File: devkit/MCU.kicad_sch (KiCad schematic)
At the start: 41 parts, among them IC601 FAN5622SX, IC602 USBLC6-2P6, IC603 MX25U51245GZ4I00, IC604 NTS0104GU12, J601 Jumper, J602 Jumper, J603 Jumper, J604 Jumper, M601 NORA-B106, X601 DEBUG, X602 Current, X603 Device, X604 UART, X605 GPIO, X606 Current, X607 IO Current, X608 Display, X609 Current, X610 LED Current

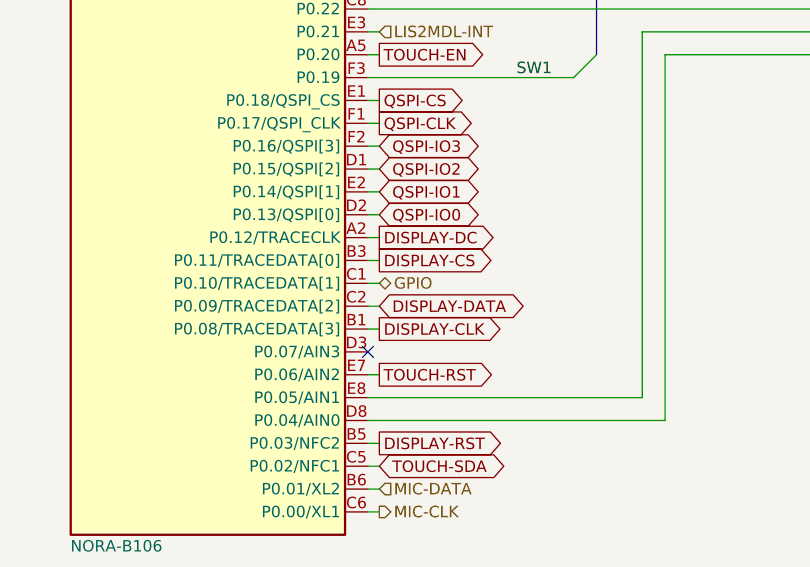
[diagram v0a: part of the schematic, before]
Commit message: Revert "Feature: Issue #180"
This reverts commit 364f4bbc8b17cbfb7f0155205af3315526997ba0.
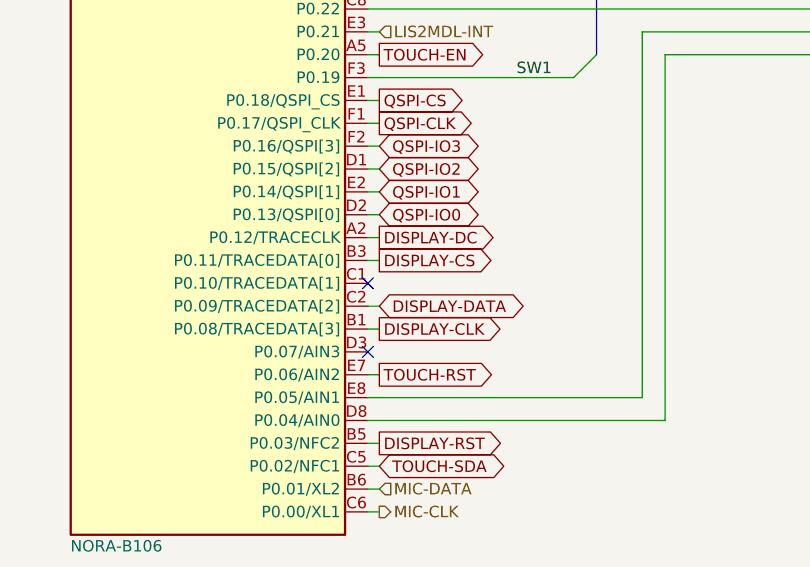
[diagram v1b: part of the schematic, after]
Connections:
- net GPIO: no longer names the net of M601.C1 (P0.10/TRACEDATA[1])
- no-connect marks 12 -> 13
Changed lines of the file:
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@@
 	)
 	(no_connect
+		(at 153.67 115.57)
+	)
+	(no_connect
 		(at 153.67 67.31)
 	)
@@
 	(wire
 		(pts
-			(xy 153.67 115.57) (xy 154.94 115.57)
-		)
-		(stroke
-			(width 0)
-			(type default)
-		)
-	)
-	(wire
-		(pts
 			(xy 124.46 181.61) (xy 124.46 210.82)
 		)
@@
 		(effects
 			(font
-				(size 1.27 1.27)
-			)
-			(justify left)
-		)
-	)
-	(hierarchical_label "GPIO"
-		(shape bidirectional)
-		(at 154.94 115.57 0)
-		(effects
-			(font

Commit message: Feature: Issue #180
- Add additional pin to I2S header

Closes #180

Signed-off-by: Daniel Kampert <DanielKampert@kampis-elektroecke.de>
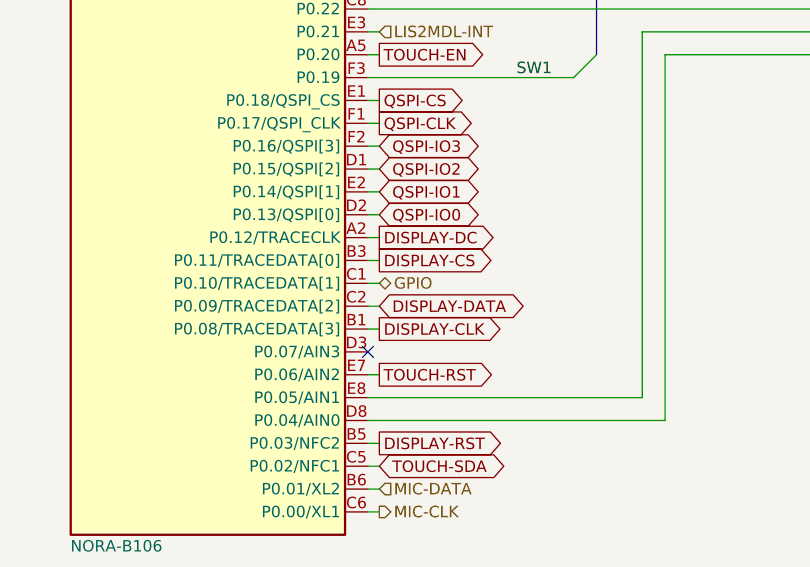
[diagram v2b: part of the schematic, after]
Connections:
- net GPIO: now reaches M601.C1 (P0.10/TRACEDATA[1])
- no-connect marks 13 -> 12
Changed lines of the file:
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@@
 	)
 	(no_connect
-		(at 153.67 115.57)
-	)
-	(no_connect
 		(at 153.67 67.31)
 	)
@@
 	(wire
 		(pts
+			(xy 153.67 115.57) (xy 154.94 115.57)
+		)
+		(stroke
+			(width 0)
+			(type default)
+		)
+	)
+	(wire
+		(pts
 			(xy 124.46 181.61) (xy 124.46 210.82)
 		)
@@
 		(effects
 			(font
+				(size 1.27 1.27)
+			)
+			(justify left)
+		)
+	)
+	(hierarchical_label "GPIO"
+		(shape bidirectional)
+		(at 154.94 115.57 0)
+		(effects
+			(font

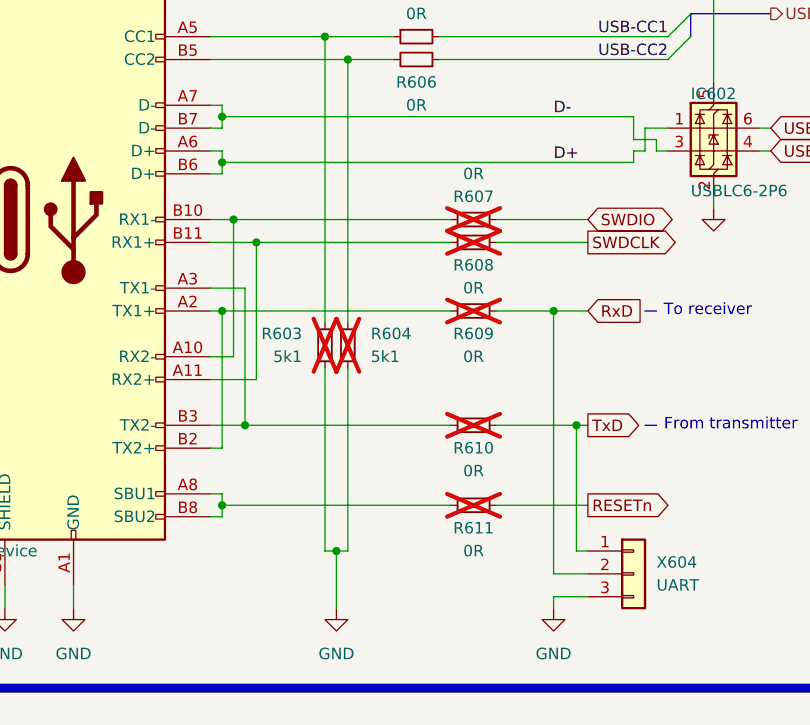
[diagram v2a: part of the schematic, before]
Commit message: Task: Issue #173
- Replace 0R with closed jumper

Closes #173

Signed-off-by: Daniel Kampert <DanielKampert@kampis-elektroecke.de>
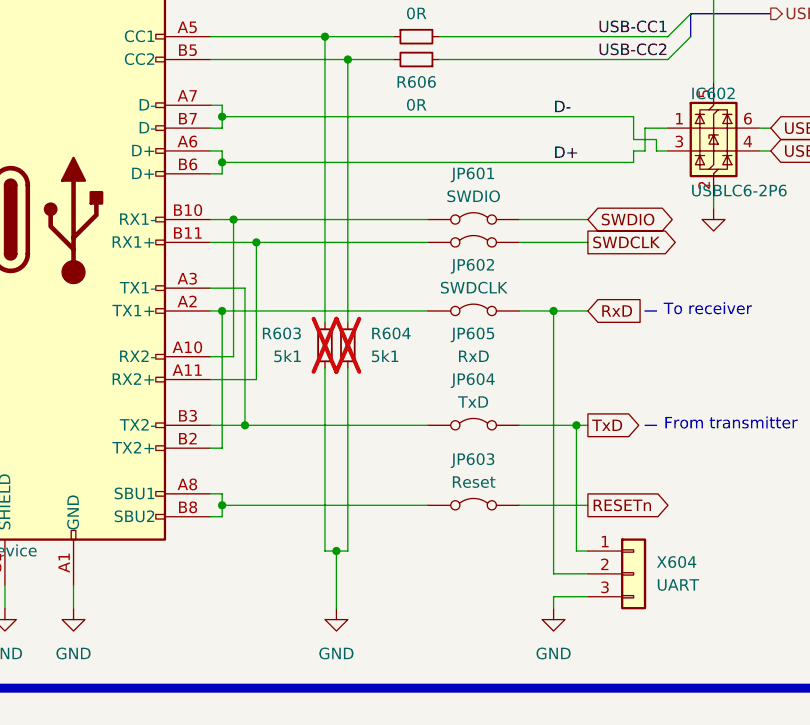
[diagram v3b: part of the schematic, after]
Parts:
- removed R607, R608, R609, R610, R611: 0R, Resistor_SMD:R_0805_2012Metric, symbol Device:R_Small
- added JP601: SWDIO, Jumper:SolderJumper-2_P1.3mm_Bridged_RoundedPad1.0x1.5mm, symbol Jumper:Jumper_2_Bridged
- added JP602: SWDCLK, Jumper:SolderJumper-2_P1.3mm_Bridged_RoundedPad1.0x1.5mm, symbol Jumper:Jumper_2_Bridged
- added JP603: Reset, Jumper:SolderJumper-2_P1.3mm_Bridged_RoundedPad1.0x1.5mm, symbol Jumper:Jumper_2_Bridged
- added JP604: TxD, Jumper:SolderJumper-2_P1.3mm_Bridged_RoundedPad1.0x1.5mm, symbol Jumper:Jumper_2_Bridged
- added JP605: RxD, Jumper:SolderJumper-2_P1.3mm_Bridged_RoundedPad1.0x1.5mm, symbol Jumper:Jumper_2_Bridged
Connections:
- net RESETn: now also JP603.2 (B)
- net RxD: now also JP605.2 (B)
- net SWDCLK: now also JP602.2 (B)
- net SWDIO: now also JP601.2 (B)
- net TxD: now also JP604.2 (B)
- net at X603.A11 (RX2+), X603.B11 (RX1+): now also JP602.1 (A)
- net at X603.A8 (SBU1), X603.B8 (SBU2): now also JP603.1 (A)
- net at X603.A10 (RX2-), X603.B10 (RX1-): now also JP601.1 (A)
- net at X603.A2 (TX1+), X603.B2 (TX2+): now also JP605.1 (A)
- net at X603.A3 (TX1-), X603.B3 (TX2-): now also JP604.1 (A)

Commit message: Revert "Task: Issue #173"
This reverts commit e04384c88487c0ad4268dbede6dd77cc14cfed5f.
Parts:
- removed JP601: SWDIO, Jumper:SolderJumper-2_P1.3mm_Bridged_RoundedPad1.0x1.5mm, symbol Jumper:Jumper_2_Bridged
- removed JP602: SWDCLK, Jumper:SolderJumper-2_P1.3mm_Bridged_RoundedPad1.0x1.5mm, symbol Jumper:Jumper_2_Bridged
- removed JP603: Reset, Jumper:SolderJumper-2_P1.3mm_Bridged_RoundedPad1.0x1.5mm, symbol Jumper:Jumper_2_Bridged
- removed JP604: TxD, Jumper:SolderJumper-2_P1.3mm_Bridged_RoundedPad1.0x1.5mm, symbol Jumper:Jumper_2_Bridged
- removed JP605: RxD, Jumper:SolderJumper-2_P1.3mm_Bridged_RoundedPad1.0x1.5mm, symbol Jumper:Jumper_2_Bridged
- added R607, R608, R609, R610, R611: 0R, Resistor_SMD:R_0805_2012Metric, symbol Device:R_Small
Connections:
- net RESETn: now also R611.1
- net RxD: now also R609.1
- net SWDCLK: now also R608.1
- net SWDIO: now also R607.1
- net TxD: now also R610.1
- net at X603.A8 (SBU1), X603.B8 (SBU2): now also R611.2
- net at X603.A2 (TX1+), X603.B2 (TX2+): now also R609.2
- net at X603.A10 (RX2-), X603.B10 (RX1-): now also R607.2
- net at X603.A11 (RX2+), X603.B11 (RX1+): now also R608.2
- net at X603.A3 (TX1-), X603.B3 (TX2-): now also R610.2
